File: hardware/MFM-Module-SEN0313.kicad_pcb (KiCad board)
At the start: 2 copper layers, 50 x 25 mm, 13 parts, among them J1 Program_conn, J2 Module board, J3 SEN0313 Header, Q1 Q_NMOS_GSD, Q2 Q_PMOS_GSD, SW1 PER_RESET, U1 ATtiny814-SS, U2 DS18B20

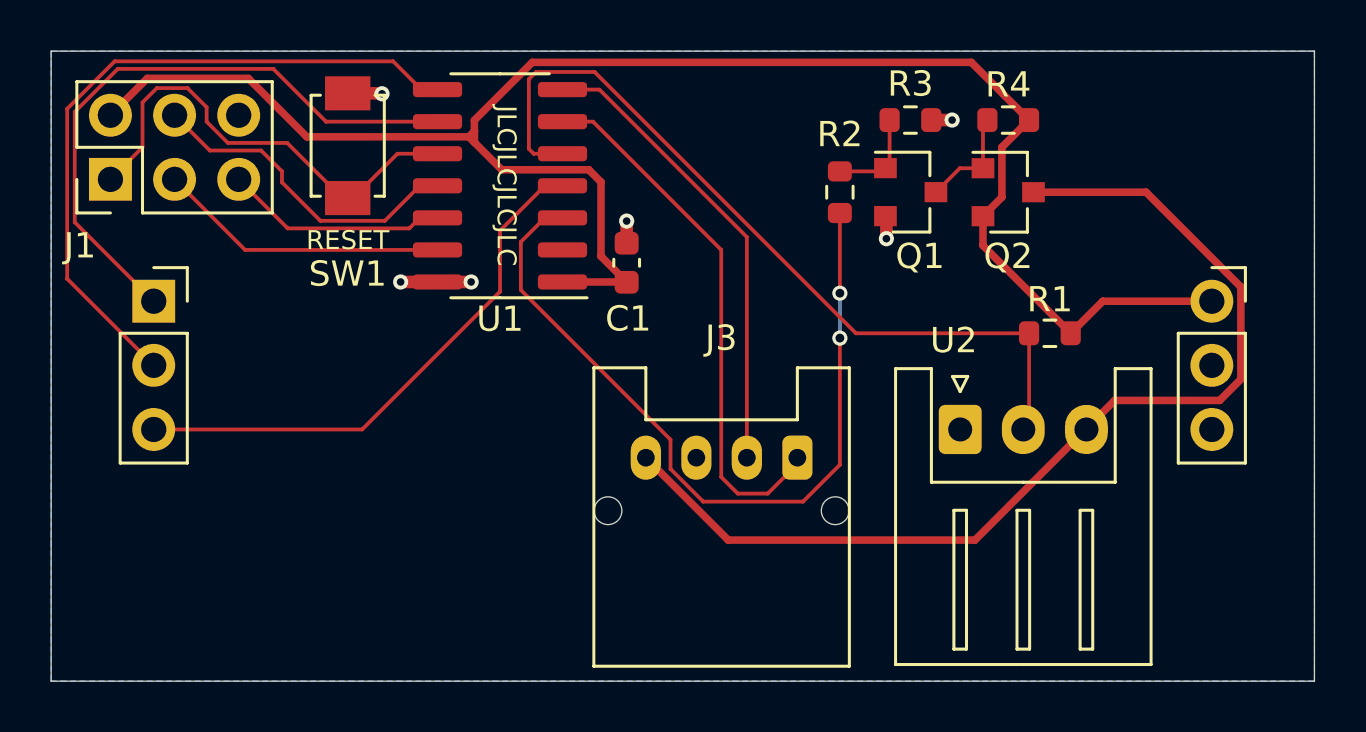
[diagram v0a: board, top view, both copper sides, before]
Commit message: update BOM with production components. Updated PCB accordingly.
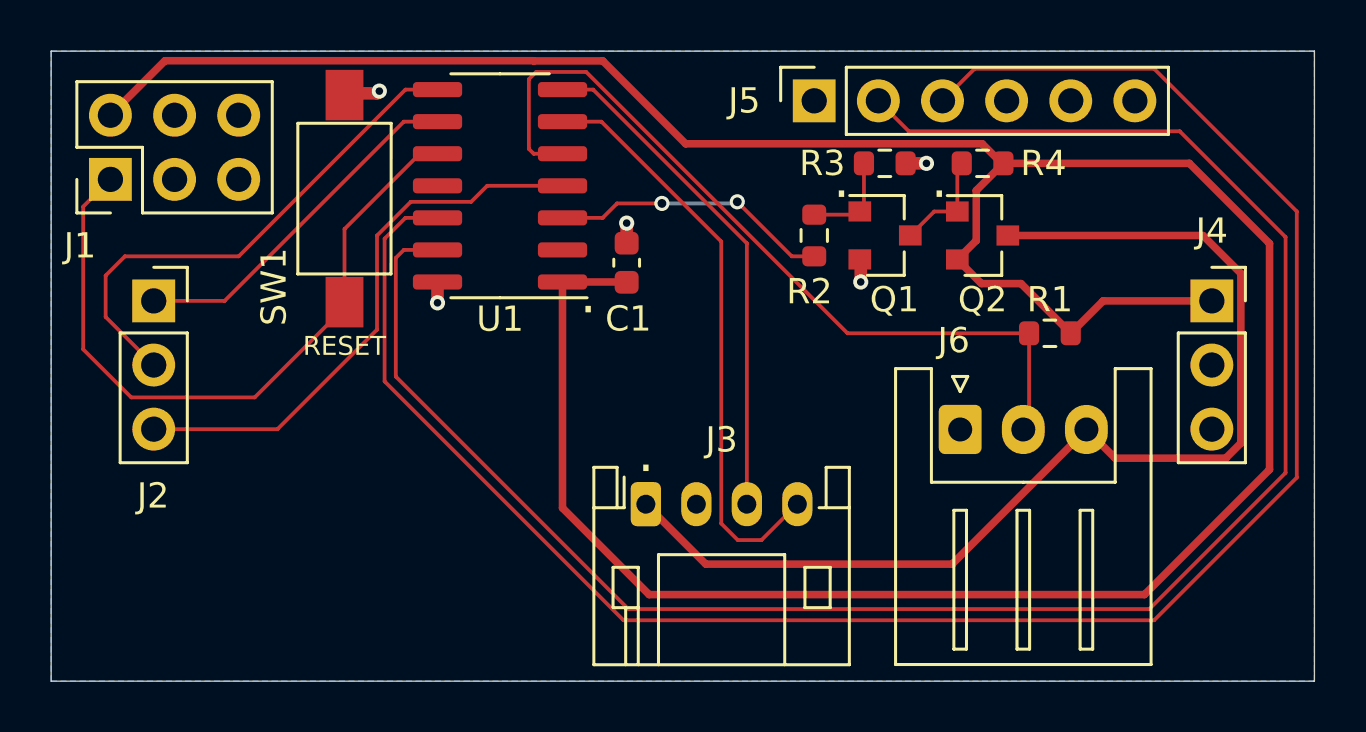
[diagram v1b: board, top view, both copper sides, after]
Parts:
- added J4: MFM Module-Right, Connector_PinSocket_2.54mm:PinSocket_1x03_P2.54mm_Vertical, F.Cu at (182.8, 86.9)
- added J5: UART Debug Connector, Connector_PinSocket_2.54mm:PinSocket_1x06_P2.54mm_Vertical, F.Cu at (167.0, 79.0)
- J2: value Module board -> MFM Module-Left; footprint custom_library_FP:MFM_Module_Board -> custom_library_FP:MFM_Module_Board_P123
- J3: footprint custom_library_FP:JST_PA_S04B-PASK-2_1x04_P2.00mm_Horizontal -> Connector_JST:JST_PH_S4B-PH-K_1x04_P2.00mm_Horizontal
- SW1: footprint custom_library_FP:SW_SPST_JLC -> custom_library_FP:SW_SPST_PTS636
- moved J2 10.7 mm to (140.8, 86.9)
- moved SW1 2.10 mm to (148.4, 82.9)
- moved Q1 1.99 mm to (169.8, 84.3)
- moved Q2 1.99 mm to (173.7, 84.3)
- moved R2 1.99 mm to (167.0, 84.3)
- moved R3 1.99 mm to (169.8, 81.5)
- moved R4 1.99 mm to (173.7, 81.5)
- moved J3 1.84 mm to (160.3, 95.0)
- renumbered U2 to J6
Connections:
- J1 pad 3: SCK -> (no net)
- J1 pad 4: MOSI -> (no net)
- J1 pad 5: MISO -> (no net)
- J3 pad 1: MCU_RX -> +3V3_SW
- J3 pad 2: MCU_TX -> GND
- J3 pad 3: GND -> MCU_TX
- J3 pad 4: +3V3_SW -> MCU_RX
- U1 pad 11: MOSI -> (no net)
- U1 pad 12: MISO -> MCU_RX_DEBUG
- U1 pad 13: SCK -> MCU_TX_DEBUG
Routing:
- net MCU_RX_DEBUG: track 0.00 -> 77.9 mm
- net MCU_TX_DEBUG: track 0.00 -> 75.5 mm
- net +3V3: track 70.5 -> 118.2 mm
- net SENSORS_ON: track 31.3 -> 11.1 mm
- net MOSI: track 13.4 -> 0.00 mm
- net SCK: track 11.6 -> 0.00 mm
- net I2C_SCL: track 24.8 -> 14.2 mm
- net RESET: track 18.4 -> 27.8 mm
- net MISO: track 8.85 -> 0.00 mm
- net I2C_SDA: track 27.5 -> 20.5 mm
- net +3V3_SW: track 41.0 -> 44.1 mm
- net GND: track 6.77 -> 4.65 mm, vias 6 -> 5
- net MCU_RX: track 21.4 -> 23.3 mm
- net MCU_TX: track 18.5 -> 20.2 mm
- net SMBALERT: track 21.6 -> 22.4 mm
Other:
- board text added: "."
- board text added: "MFM Module SEN0313 v0.2 2021-05-24 Senwize"
- board text removed: "JLCJLCJLCJLC"
- board text removed: "MFM Module SEN0313 v0.1 2021-05-08 Senwize"
- board text removed: "MISO"
- board text removed: "MOSI"
- board text removed: "SCK"

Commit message: ready for production (@Productronics)
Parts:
- J3: footprint Connector_JST:JST_PH_S4B-PH-K_1x04_P2.00mm_Horizontal -> custom_library_FP:JST_PA_S04B-PASK-2_1x04_P2.00mm_Horizontal
- U1: value ATtiny814-SS -> ATtiny1614-SS
- moved J3 1.97 mm to (160.7, 93.0)
- moved U1 0.06 mm to (154.5, 82.4)
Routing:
- net +3V3_SW: track 44.1 -> 36.1 mm
- net MCU_RX: track 23.3 -> 17.1 mm
- net MCU_TX: track 20.2 -> 17.6 mm
- net +3V3: track 118.2 -> 116.6 mm
- net ONEWIRE: track 32.4 -> 31.3 mm
- net MCU_TX_DEBUG: track 75.5 -> 74.4 mm
- net MCU_RX_DEBUG: track 77.9 -> 78.6 mm
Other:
- board text added: "MCU-RX"
- board text added: "MCU-TX"
- board text added: "MFM Module SEN0313 v0.2 2021-10-09 Senwize B.V."
- board text removed: "MFM Module SEN0313 v0.2 2021-05-24 Senwize"
- board text removed: "RX"
- board text removed: "TX"
